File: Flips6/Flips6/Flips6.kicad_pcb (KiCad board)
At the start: 2 copper layers, 24 parts, among them CN201 Conn_02x05_Odd_Even, CN301 Conn_02x05_Odd_Even, CN401 Conn_02x05_Odd_Even, CN501 Conn_02x05_Odd_Even, CN601 Conn_02x05_Odd_Even, CN701 Conn_02x05_Odd_Even, CN801 Conn_02x05_Odd_Even, J101 Conn_02x04_Odd_Even, U201 74HCT595, U301 74HCT595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

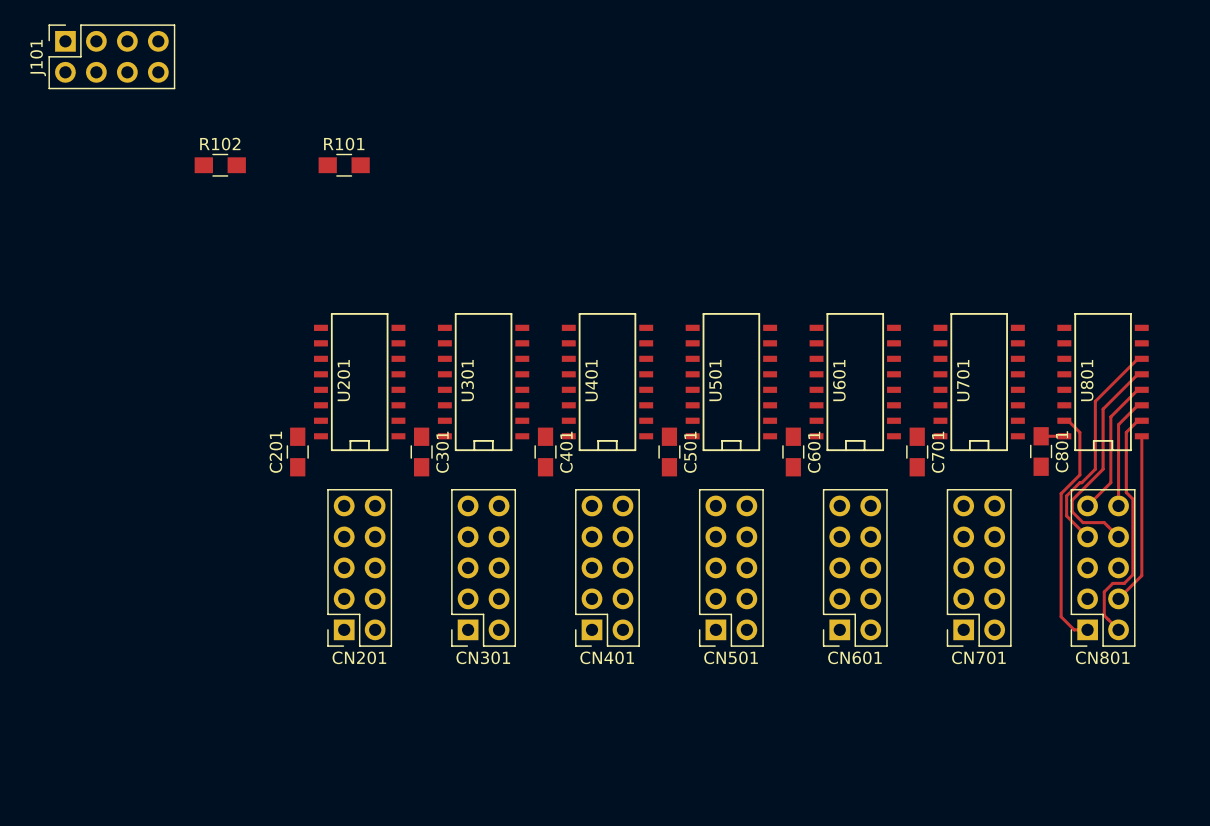
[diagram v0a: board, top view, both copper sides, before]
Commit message: Finished routing for Fips6 first attempt
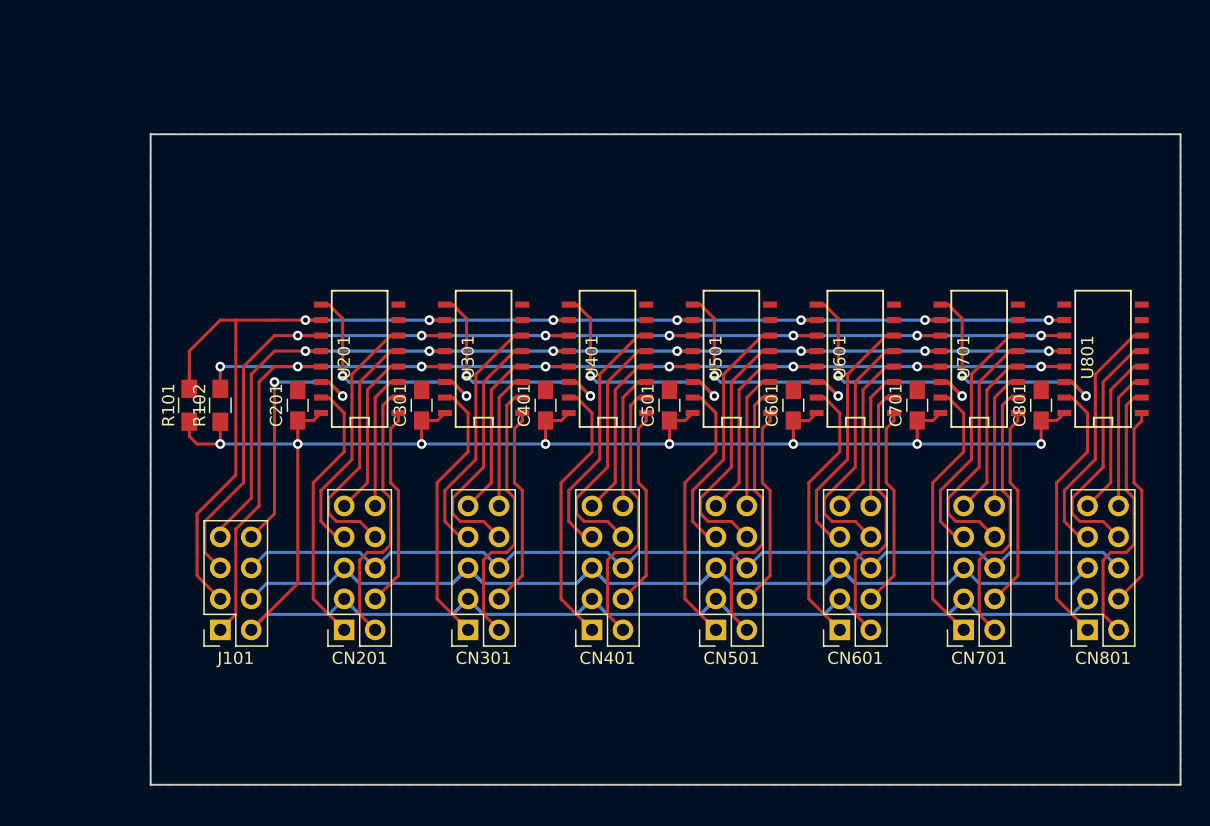
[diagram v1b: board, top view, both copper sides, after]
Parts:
- moved J101 49.9 mm to (182.9, 94.0), turned to 180 degrees
- moved R101 23.4 mm to (180.3, 75.6), turned to 90 degrees
- moved R102 19.7 mm to (182.9, 75.6), turned to 90 degrees
- moved C201 3.83 mm to (189.2, 75.6)
- moved C301 3.83 mm to (199.4, 75.6), turned to 90 degrees
- moved C401 3.83 mm to (209.6, 75.6), turned to 90 degrees
- moved C501 3.83 mm to (219.7, 75.6), turned to 90 degrees
- moved C601 3.83 mm to (229.9, 75.6), turned to 90 degrees
- moved C701 3.83 mm to (240.0, 75.6), turned to 90 degrees
- moved C801 3.79 mm to (250.2, 75.6), turned to 90 degrees
- moved U201 1.91 mm to (194.3, 71.8)
- moved U301 1.91 mm to (204.5, 71.8)
- moved U401 1.91 mm to (214.6, 71.8)
- moved U501 1.91 mm to (224.8, 71.8)
- moved U601 1.91 mm to (234.9, 71.8)
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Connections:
- CN701 pad 1: /ShiftRegister1/A0 -> /ShiftRegister7/A0
- CN701 pad 10: /ShiftRegister1/B0 -> /ShiftRegister7/B0
- CN701 pad 2: /ShiftRegister1/A2 -> /ShiftRegister7/A2
- CN701 pad 4: /ShiftRegister1/A1 -> /ShiftRegister7/A1
- CN701 pad 7: /ShiftRegister1/EN -> /ShiftRegister7/EN
- CN701 pad 8: /ShiftRegister1/DATA -> /ShiftRegister7/DATA
- CN701 pad 9: /ShiftRegister1/B1 -> /ShiftRegister7/B1
- CN801 pad 1: /ShiftRegister7/A0 -> /ShiftRegister8/A0
- CN801 pad 10: /ShiftRegister7/B0 -> /ShiftRegister8/B0
- CN801 pad 2: /ShiftRegister7/A2 -> /ShiftRegister8/A2
- CN801 pad 4: /ShiftRegister7/A1 -> /ShiftRegister8/A1
- CN801 pad 7: /ShiftRegister7/EN -> /ShiftRegister8/EN
- CN801 pad 8: /ShiftRegister7/DATA -> /ShiftRegister8/DATA
- CN801 pad 9: /ShiftRegister7/B1 -> /ShiftRegister8/B1
- J101 pad 2: +12V -> +5V
- J101 pad 3: SRCLK -> ~SRCLR
- J101 pad 4: +5V -> +12V
- J101 pad 5: ~SRCLR -> SRCLK
- J101 pad 8: /ShiftRegister1/DIN -> /ShiftRegister2/DIN
- U201 pad 7: Net-(U201-Pad7) -> (no net)
- U301 pad 7: Net-(U301-Pad7) -> (no net)
- U401 pad 7: Net-(U401-Pad7) -> (no net)
- U501 pad 7: Net-(U501-Pad7) -> (no net)
- U601 pad 7: Net-(U601-Pad7) -> (no net)
- U701 pad 1: /ShiftRegister1/A1 -> /ShiftRegister7/A1
- U701 pad 14: /ShiftRegister1/DIN -> /ShiftRegister7/DIN
- U701 pad 15: /ShiftRegister1/A0 -> /ShiftRegister7/A0
- U701 pad 2: /ShiftRegister1/A2 -> /ShiftRegister7/A2
- U701 pad 3: /ShiftRegister1/B0 -> /ShiftRegister7/B0
- U701 pad 4: /ShiftRegister1/B1 -> /ShiftRegister7/B1
- U701 pad 5: /ShiftRegister1/DATA -> /ShiftRegister7/DATA
- U701 pad 6: /ShiftRegister1/EN -> /ShiftRegister7/EN
- U701 pad 7: Net-(U701-Pad7) -> (no net)
- U701 pad 9: /ShiftRegister2/DIN -> /ShiftRegister8/DIN
- U801 pad 1: /ShiftRegister7/A1 -> /ShiftRegister8/A1
- U801 pad 14: /ShiftRegister7/DIN -> /ShiftRegister8/DIN
- U801 pad 15: /ShiftRegister7/A0 -> /ShiftRegister8/A0
- U801 pad 2: /ShiftRegister7/A2 -> /ShiftRegister8/A2
- U801 pad 3: /ShiftRegister7/B0 -> /ShiftRegister8/B0
- U801 pad 4: /ShiftRegister7/B1 -> /ShiftRegister8/B1
- U801 pad 5: /ShiftRegister7/DATA -> /ShiftRegister8/DATA
- U801 pad 6: /ShiftRegister7/EN -> /ShiftRegister8/EN
- U801 pad 7: Net-(U801-Pad7) -> (no net)
- U801 pad 9: /ShiftRegister7/DOUT -> (no net)
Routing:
- net +5V: track 1.91 -> 211.1 mm, vias 0 -> 8
- net ~SRCLR: track 0.00 -> 109.7 mm, vias 0 -> 7
- net ~OE: track 0.00 -> 107.8 mm, vias 0 -> 8
- net SRCLK: track 0.00 -> 98.1 mm, vias 0 -> 7
- net +12V: track 0.00 -> 89.5 mm
- net RCLK: track 0.00 -> 89.5 mm, vias 0 -> 7
- net GND: track 0.00 -> 78.5 mm
- net /ShiftRegister6/A2: track 0.00 -> 22.5 mm
- net /ShiftRegister5/A2: track 0.00 -> 22.5 mm
- net /ShiftRegister4/A2: track 0.00 -> 22.5 mm
- net /ShiftRegister3/A2: track 0.00 -> 22.5 mm
- net /ShiftRegister2/A2: track 0.00 -> 22.5 mm
- net /ShiftRegister8/A2: track 0.00 -> 22.5 mm
- net /ShiftRegister6/A0: track 0.00 -> 22.3 mm
- net /ShiftRegister5/A0: track 0.00 -> 22.3 mm
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- added copper zone on B.Cu, net GND
- added copper zone on F.Cu, net GND
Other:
- board outline added: 84.5 x 53.3 mm

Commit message: Making shape 90x50, with mounting holes in 80x40 rectangle
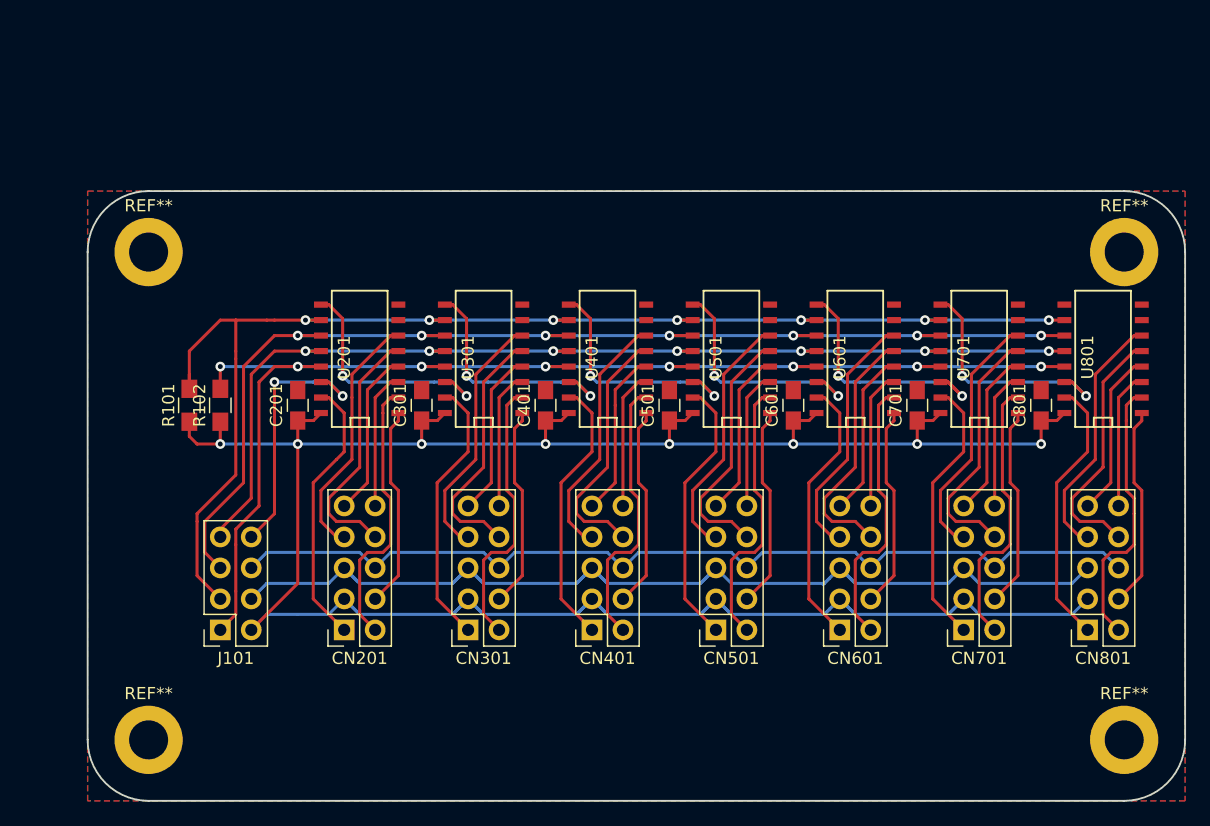
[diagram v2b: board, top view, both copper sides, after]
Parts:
- added REF**: MountingHole_3.2mm_M3_DIN965_Pad, Mounting_Holes:MountingHole_3.2mm_M3_DIN965_Pad, F.Cu at (257.0, 63.0)
- added REF**: MountingHole_3.2mm_M3_DIN965_Pad, Mounting_Holes:MountingHole_3.2mm_M3_DIN965_Pad, F.Cu at (177.0, 63.0)
- added REF**: MountingHole_3.2mm_M3_DIN965_Pad, Mounting_Holes:MountingHole_3.2mm_M3_DIN965_Pad, F.Cu at (177.0, 103.0)
- added REF**: MountingHole_3.2mm_M3_DIN965_Pad, Mounting_Holes:MountingHole_3.2mm_M3_DIN965_Pad, F.Cu at (257.0, 103.0)
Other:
- board size 84.5 x 53.3 mm -> 90 x 50 mm
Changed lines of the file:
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@@
   (general
     (thickness 1.6)
-    (drawings 17)
+    (drawings 25)
     (tracks 656)
     (zones 0)
-    (modules 24)
+    (modules 28)
     (nets 64)
   )
@@
     (add_net ~SRCLR)
   )
+  (module Mounting_Holes:MountingHole_3.2mm_M3_DIN965_Pad (layer F.Cu)
+    (at 257 63)
+    (descr "Mounting Hole 3.2mm, M3, DIN965")
+    (tags "mounting hole 3.2mm m3 din965")
+    (attr virtual)
+    (fp_text reference REF** (at 0 -3.8) (layer F.SilkS)
+      (effects (font (size 1 1) (thickness 0.15)))
+    )
+    (fp_text value MountingHole_3.2mm_M3_DIN965_Pad (at 0 3.8) (layer F.Fab)
+      (effects (font (size 1 1) (thickness 0.15)))
+    )
+    (fp_text user %R (at 0.3 0) (layer F.Fab)
+      (effects (font (size 1 1) (thickness 0.15)))
+    )
+    (fp_circle (center 0 0) (end 2.8 0) (layer Cmts.User) (width 0.15))
+    (fp_circle (center 0 0) (end 3.05 0) (layer F.CrtYd) (width 0.05))
+    (pad 1 thru_hole circle (at 0 0) (size 5.6 5.6) (drill 3.2) (layers *.Cu *.Mask))
+  )
+  (module Mounting_Holes:MountingHole_3.2mm_M3_DIN965_Pad (layer F.Cu)
+    (at 177 63)
+    (descr "Mounting Hole 3.2mm, M3, DIN965")
+    (tags "mounting hole 3.2mm m3 din965")
+    (attr virtual)
+    (fp_text reference REF** (at 0 -3.8) (layer F.SilkS)
+      (effects (font (size 1 1) (thickness 0.15)))
+    )
+    (fp_text value MountingHole_3.2mm_M3_DIN965_Pad (at 0 3.8) (layer F.Fab)
+      (effects (font (size 1 1) (thickness 0.15)))
+    )
+    (fp_text user %R (at 0.3 0) (layer F.Fab)
+      (effects (font (size 1 1) (thickness 0.15)))
+    )
+    (fp_circle (center 0 0) (end 2.8 0) (layer Cmts.User) (width 0.15))
+    (fp_circle (center 0 0) (end 3.05 0) (layer F.CrtYd) (width 0.05))
+    (pad 1 thru_hole circle (at 0 0) (size 5.6 5.6) (drill 3.2) (layers *.Cu *.Mask))
+  )
+  (module Mounting_Holes:MountingHole_3.2mm_M3_DIN965_Pad (layer F.Cu)
+    (at 177 103)
+    (descr "Mounting Hole 3.2mm, M3, DIN965")
+    (tags "mounting hole 3.2mm m3 din965")
+    (attr virtual)
+    (fp_text reference REF** (at 0 -3.8) (layer F.SilkS)
+      (effects (font (size 1 1) (thickness 0.15)))
+    )
+    (fp_text value MountingHole_3.2mm_M3_DIN965_Pad (at 0 3.8) (layer F.Fab)
+      (effects (font (size 1 1) (thickness 0.15)))
+    )
+    (fp_text user %R (at 0.3 0) (layer F.Fab)
+      (effects (font (size 1 1) (thickness 0.15)))
+    )
+    (fp_circle (center 0 0) (end 2.8 0) (layer Cmts.User) (width 0.15))
+    (fp_circle (center 0 0) (end 3.05 0) (layer F.CrtYd) (width 0.05))
+    (pad 1 thru_hole circle (at 0 0) (size 5.6 5.6) (drill 3.2) (layers *.Cu *.Mask))
+  )
+  (module Mounting_Holes:MountingHole_3.2mm_M3_DIN965_Pad (layer F.Cu)
+    (at 257 103)
+    (descr "Mounting Hole 3.2mm, M3, DIN965")
+    (tags "mounting hole 3.2mm m3 din965")
+    (attr virtual)
+    (fp_text reference REF** (at 0 -3.8) (layer F.SilkS)
+      (effects (font (size 1 1) (thickness 0.15)))
+    )
+    (fp_text value MountingHole_3.2mm_M3_DIN965_Pad (at 0 3.8) (layer F.Fab)
+      (effects (font (size 1 1) (thickness 0.15)))
+    )
+    (fp_text user %R (at 0.3 0) (layer F.Fab)
+      (effects (font (size 1 1) (thickness 0.15)))
+    )
+    (fp_circle (center 0 0) (end 2.8 0) (layer Cmts.User) (width 0.15))
+    (fp_circle (center 0 0) (end 3.05 0) (layer F.CrtYd) (width 0.05))
+    (pad 1 thru_hole circle (at 0 0) (size 5.6 5.6) (drill 3.2) (layers *.Cu *.Mask))
+  )
   (module Capacitors_SMD:C_0805_HandSoldering (layer F.Cu)
     (at 189.23 75.565 90)
@@
     )
   )
+  (dimension 90 (width 0.3) (layer Dwgs.User)
+    (gr_text "90,000 mm" (at 216.972996 36.884528) (layer Dwgs.User)
+      (effects (font (size 1.5 1.5) (thickness 0.3)))
+    )
+    (feature1 (pts (xy 171.972996 55.984528) (xy 171.972996 38.398107)))
+    (feature2 (pts (xy 261.972996 55.984528) (xy 261.972996 38.398107)))
+    (crossbar (pts (xy 261.972996 38.984528) (xy 171.972996 38.984528)))
+    (arrow1a (pts (xy 171.972996 38.984528) (xy 173.0995 38.398107)))
+    (arrow1b (pts (xy 171.972996 38.984528) (xy 173.0995 39.570949)))
+    (arrow2a (pts (xy 261.972996 38.984528) (xy 260.846492 38.398107)))
+    (arrow2b (pts (xy 261.972996 38.984528) (xy 260.846492 39.570949)))
+  )
+  (dimension 80 (width 0.3) (layer Dwgs.User)
+    (gr_text "80,000 mm" (at 217.011494 44.9) (layer Dwgs.User)
+      (effects (font (size 1.5 1.5) (thickness 0.3)))
+    )
+    (feature1 (pts (xy 177.011494 56) (xy 177.011494 46.413579)))
+    (feature2 (pts (xy 257.011494 56) (xy 257.011494 46.413579)))
+    (crossbar (pts (xy 257.011494 47) (xy 177.011494 47)))
+    (arrow1a (pts (xy 177.011494 47) (xy 178.137998 46.413579)))
+    (arrow1b (pts (xy 177.011494 47) (xy 178.137998 47.586421)))
+    (arrow2a (pts (xy 257.011494 47) (xy 255.88499 46.413579)))
+    (arrow2b (pts (xy 257.011494 47) (xy 255.88499 47.586421)))
+  )
+  (dimension 40 (width 0.3) (layer Dwgs.User)
+    (gr_text "40,000 mm" (at 276.948337 83 90) (layer Dwgs.User)
+      (effects (font (size 1.5 1.5) (thickness 0.3)))
+    )
+    (feature1 (pts (xy 263.848337 63) (xy 275.434758 63)))
+    (feature2 (pts (xy 263.848337 103) (xy 275.434758 103)))
+    (crossbar (pts (xy 274.848337 103) (xy 274.848337 63)))
+    (arrow1a (pts (xy 274.848337 63) (xy 275.434758 64.126504)))
+    (arrow1b (pts (xy 274.848337 63) (xy 274.261916 64.126504)))
+    (arrow2a (pts (xy 274.848337 103) (xy 275.434758 101.873496)))
+    (arrow2b (pts (xy 274.848337 103) (xy 274.261916 101.873496)))
+  )
+  (dimension 50 (width 0.3) (layer Dwgs.User)
+    (gr_text "50,000 mm" (at 282.902539 83.028963 90) (layer Dwgs.User)
+      (effects (font (size 1.5 1.5) (thickness 0.3)))
+    )
+    (feature1 (pts (xy 263.802539 58.028963) (xy 281.38896 58.028963)))
+    (feature2 (pts (xy 263.802539 108.028963) (xy 281.38896 108.028963)))
+    (crossbar (pts (xy 280.802539 108.028963) (xy 280.802539 58.028963)))
+    (arrow1a (pts (xy 280.802539 58.028963) (xy 281.38896 59.155467)))
+    (arrow1b (pts (xy 280.802539 58.028963) (xy 280.216118 59.155467)))
+    (arrow2a (pts (xy 280.802539 108.028963) (xy 281.38896 106.902459)))
+    (arrow2b (pts (xy 280.802539 108.028963) (xy 280.216118 106.902459)))
+  )
+  (gr_arc (start 177 103) (end 172 103) (angle -90) (layer Edge.Cuts) (width 0.15))
+  (gr_arc (start 177 63) (end 177 58) (angle -90) (layer Edge.Cuts) (width 0.15))
+  (gr_arc (start 257 63) (end 262 63) (angle -90) (layer Edge.Cuts) (width 0.15))
+  (gr_arc (start 257 103) (end 257 108) (angle -90) (layer Edge.Cuts) (width 0.15))
+  (gr_line (start 262 63) (end 262 103) (layer Edge.Cuts) (width 0.15))
+  (gr_line (start 177 58) (end 257 58) (layer Edge.Cuts) (width 0.15))
+  (gr_line (start 172 103) (end 172 63) (layer Edge.Cuts) (width 0.15))
+  (gr_line (start 257 108) (end 177 108) (layer Edge.Cuts) (width 0.15))
   (gr_line (start 179.07 78.105) (end 189.23 78.105) (layer B.SilkS) (width 0.2))
   (gr_line (start 179.07 99.695) (end 179.07 78.105) (layer B.SilkS) (width 0.2))
   (gr_line (start 189.23 99.695) (end 179.07 99.695) (layer B.SilkS) (width 0.2))
-  (gr_line (start 177.165 106.68) (end 177.165 53.34) (angle 90) (layer Edge.Cuts) (width 0.15))
-  (gr_line (start 261.62 106.68) (end 177.165 106.68) (angle 90) (layer Edge.Cuts) (width 0.15))
-  (gr_line (start 261.62 53.34) (end 261.62 106.68) (angle 90) (layer Edge.Cuts) (width 0.15))
-  (gr_line (start 177.165 53.34) (end 261.62 53.34) (angle 90) (layer Edge.Cuts) (width 0.15))
   (gr_line (start 199.39 78.105) (end 199.39 99.695) (layer Margin) (width 0.2))
   (gr_line (start 209.55 99.695) (end 209.55 78.105) (layer Margin) (width 0.2))
@@
     (polygon
       (pts
-        (xy 261.62 53.34) (xy 261.62 106.68) (xy 177.165 106.68) (xy 177.165 53.34)
+        (xy 262 58) (xy 262 108) (xy 172 108) (xy 172 58)
       )
     )
@@
     (polygon
       (pts
-        (xy 261.62 53.34) (xy 261.62 106.68) (xy 177.165 106.68) (xy 177.165 53.34)
+        (xy 262 58) (xy 262 108) (xy 172 108) (xy 172 58)
       )
     )

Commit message: adding vias for GND
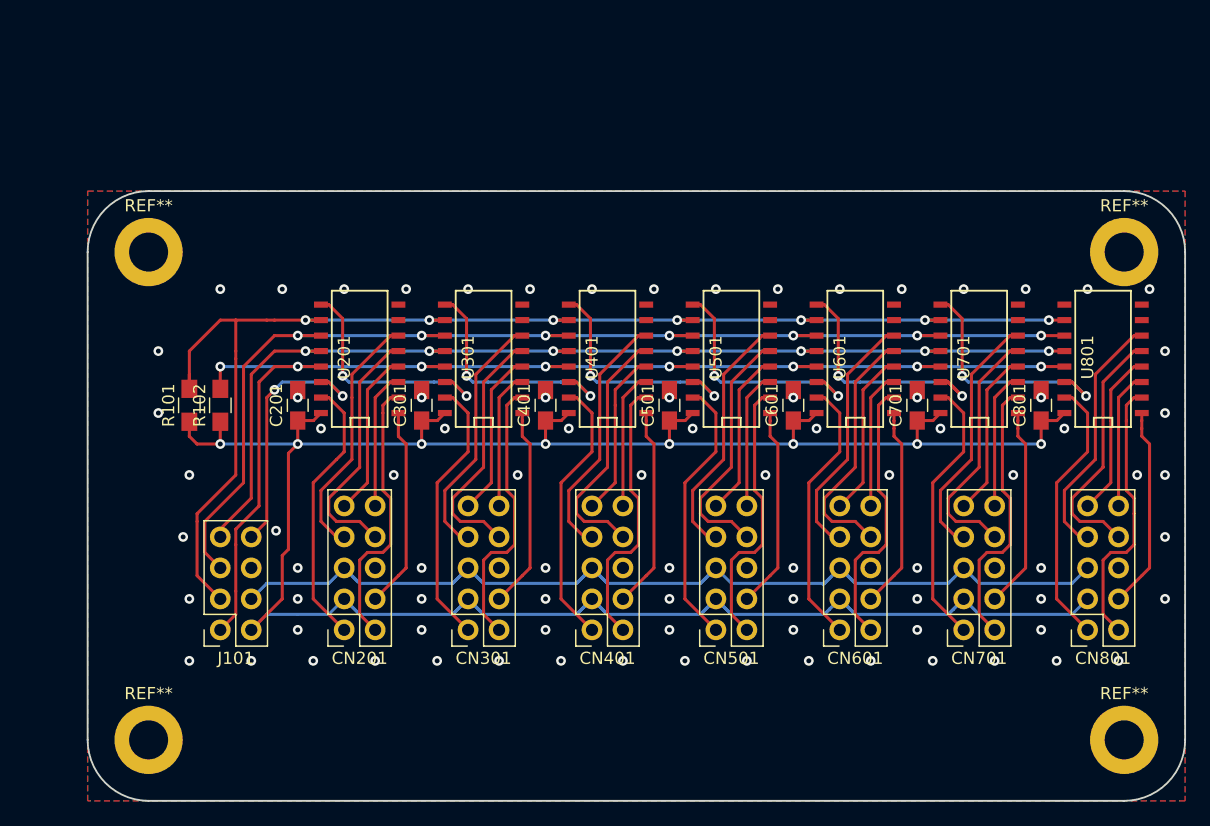
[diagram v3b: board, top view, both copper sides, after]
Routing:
- net GND: track 78.5 -> 0.00 mm, vias 0 -> 85
